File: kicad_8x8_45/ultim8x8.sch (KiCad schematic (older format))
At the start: 10 parts, among them P1 Input1, P2 Output1, P3 5V, P4 GND, P5 Input2, P6 Output2

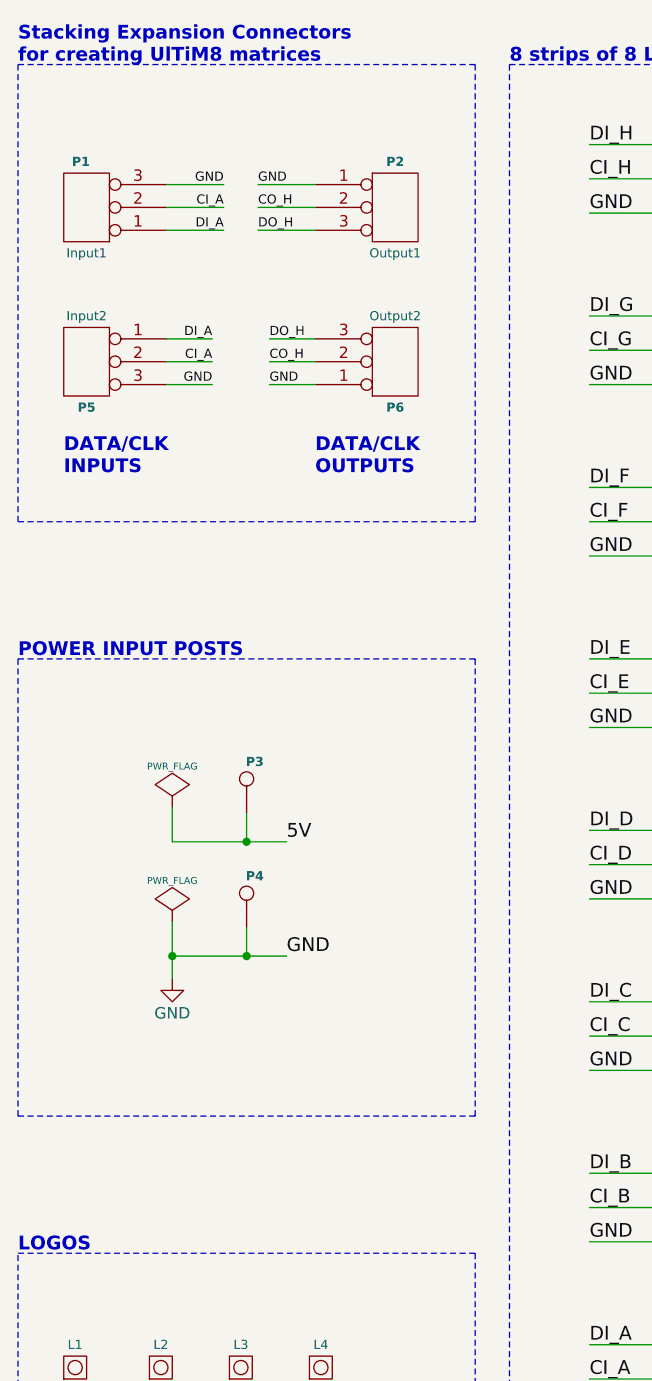
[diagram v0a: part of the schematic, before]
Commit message: angled LED version complete
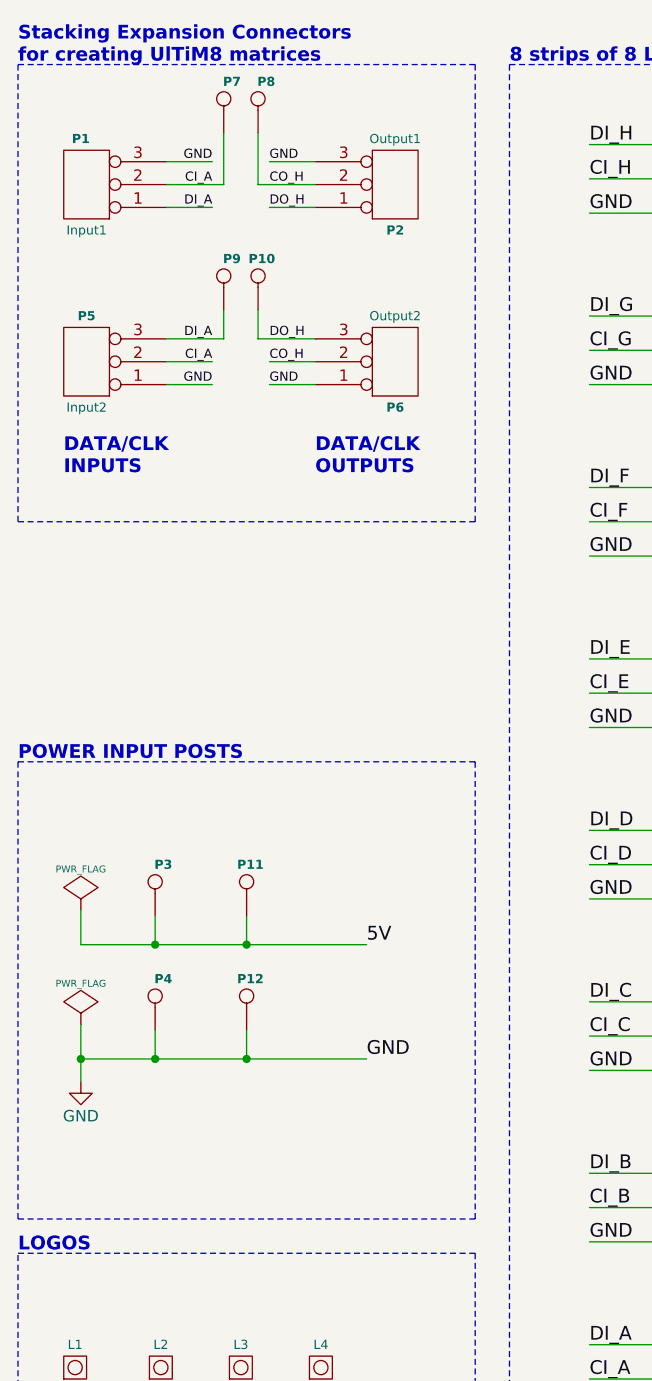
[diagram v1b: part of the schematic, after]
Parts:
- added P10: DO_H, ultim8x8_libs:Screw, symbol CONN_1
- added P11: 5V, ultim8x8_libs:Screw, symbol CONN_1
- added P12: GND, ultim8x8_libs:Screw, symbol CONN_1
- added P7: CI_A, ultim8x8_libs:Screw, symbol CONN_1
- added P8: CO_H, ultim8x8_libs:Screw, symbol CONN_1
- added P9: DI_A, ultim8x8_libs:Screw, symbol CONN_1
- P1, P2, P5, P6: footprint ultim8x8_libs:header_3pos_smd_male -> ultim8x8_libs:header_3pos_th_male
- P3, P4: footprint ultim8x8_libs:PowerIn_stud -> ultim8x8_libs:Screw
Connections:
- net 5V: now also P11.1
- net CI_A: now also P7.1
- net CO_H: now also P8.1
- net DI_A: now also P5.3 (P3), P9.1; no longer P5.1 (P1)
- net DO_H: now also P2.1 (P1), P10.1; no longer P2.3 (P3)
- net GND: now also P2.3 (P3), P5.1 (P1), P12.1; no longer P2.1 (P1), P5.3 (P3)
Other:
- moved on the sheet: P1, P2, P3, P4
